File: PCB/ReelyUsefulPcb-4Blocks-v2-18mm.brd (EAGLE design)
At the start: 50 x 86 mm, 28 parts, among them Q1 BSS138, U2 TJCTM240, U3 PHOTON_SMD

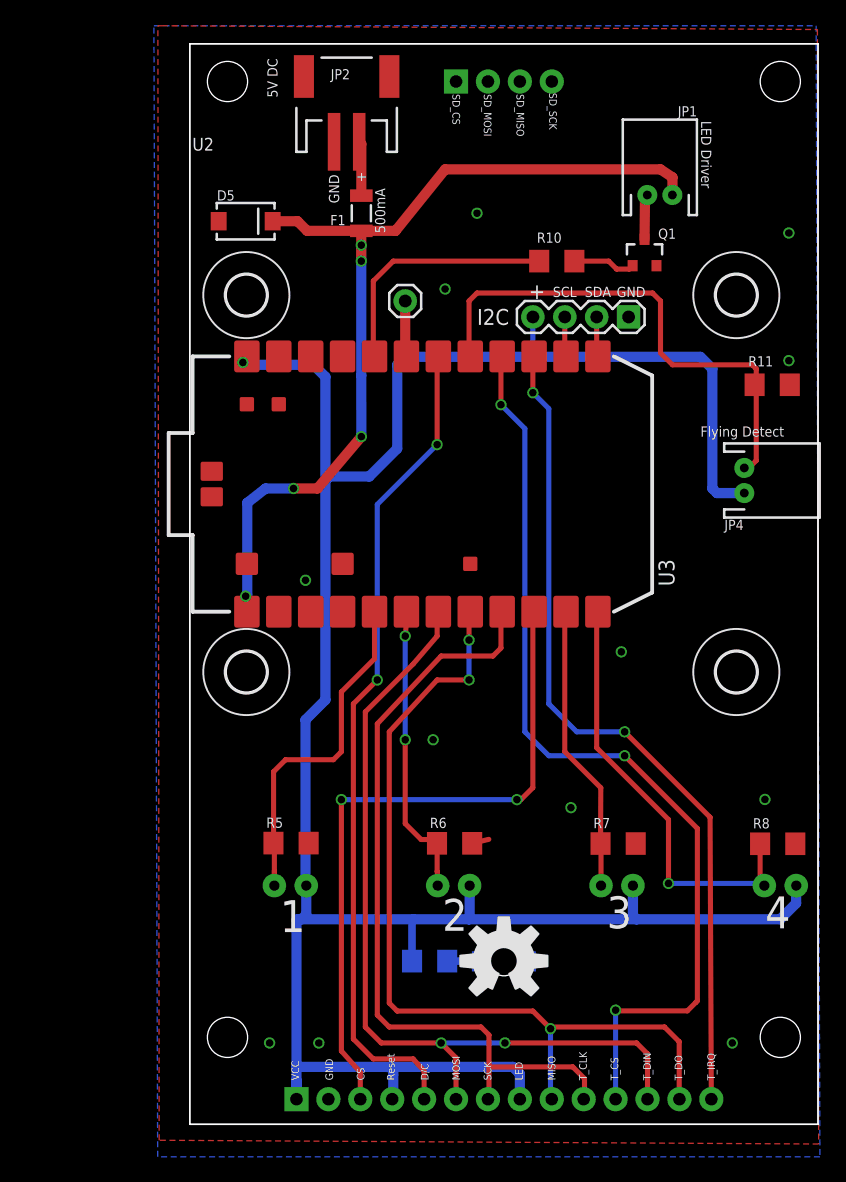
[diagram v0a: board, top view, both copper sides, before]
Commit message: Changed each spool block width to 15mm to give more space for the spools.
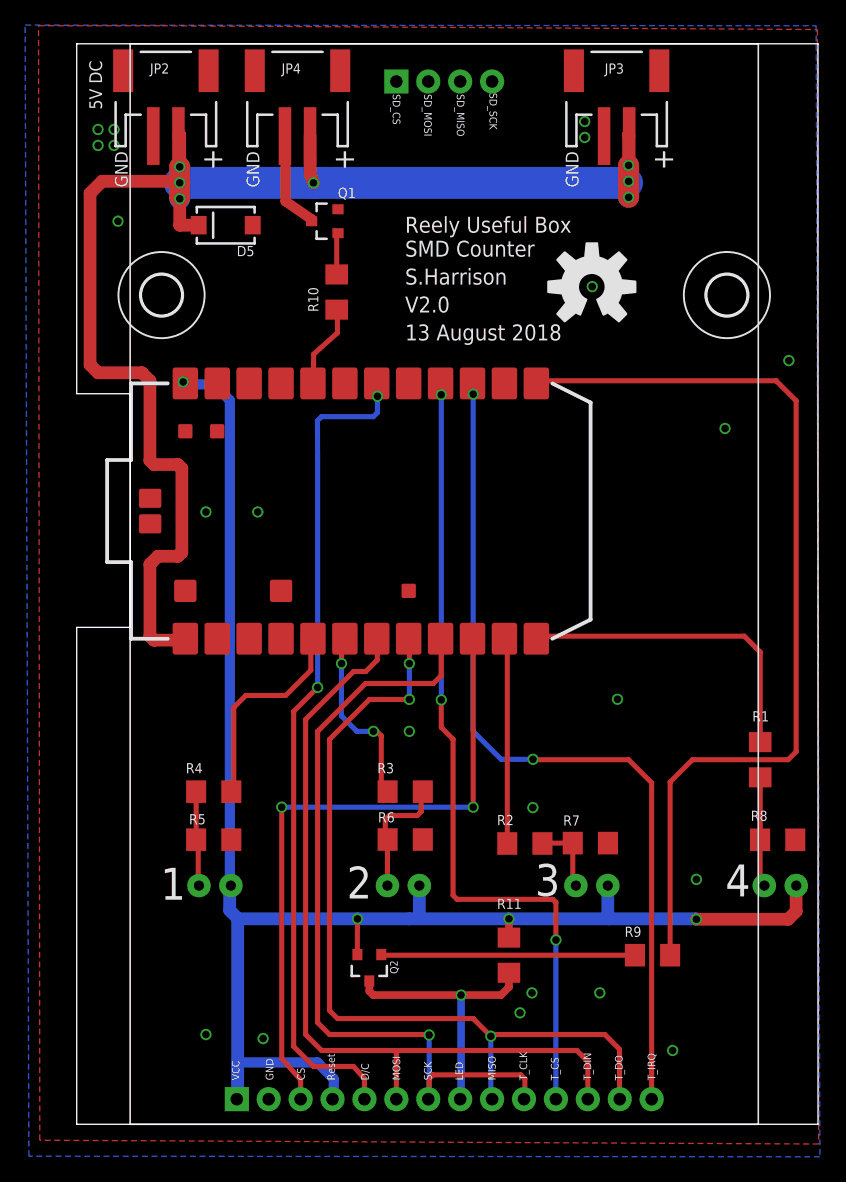
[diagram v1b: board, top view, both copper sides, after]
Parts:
- removed D10: kptd-3216qbc-d-01, SparkFun-LED:LED-1206-BOTTOM
- removed F1: 1206L200PR, SparkFun-PowerIC:PTC-1206
- removed H1, H2: MOUNT-HOLE3.2, holes:3,2
- removed JP1: LED Driver, SparkFun-Connectors:JST-2-PTH
- removed JP6: (no value), SparkFun-Connectors:1X01
- added Q2: 2.5A/30V/105mΩ, SparkFun-DiscreteSemi:SOT23-3
- added R1, R2, R3, R4: 0R, SparkFun-Resistors:1206
- JP3: value i2c -> Power Out; device SparkFun-Connectors:1X04 -> SparkFun-Connectors:JST-2-SMD
- JP4: value Flying detector -> LED Drive; device SparkFun-Connectors:JST-2-PTH -> SparkFun-Connectors:JST-2-SMD
- Q1: device SparkFun-DiscreteSemi:SOT23-3 -> SparkFun-DiscreteSemi:SOT23-3@1
- R11: value 10k -> DNP/0R
- R9: value 1k5 -> 10R
- U2: value TJCTM240 -> TJCTM240NO-MOUNTING-HOMES; device 2.8InchTFT:TJCTM240 -> 2.8InchTFT:TJCTM240-NOHOLES
- moved LOGO1 54.1 mm to (32.0, 50.7)
- moved R11 50.0 mm to (25.4, -2.54), turned to 270 degrees
- moved JP4 47.3 mm to (8.57, 66.4), turned to 0 degrees
- moved Q1 25.5 mm to (10.8, 55.9), turned to 90 degrees
- moved JP3 18.1 mm to (34.0, 66.4), turned to 0 degrees
- moved R9 17.7 mm to (36.8, -2.54), flipped to the top
- moved R10 17.7 mm to (11.7, 50.2), turned to 90 degrees
- moved JP2 14.4 mm to (-1.91, 66.4)
- moved H3 6.75 mm to (-2.25, 50.0)
- moved R5 6.16 mm to (1.91, 6.65)
- moved D1 6.00 mm to (2.00, 3.00)
- moved U3 5.35 mm to (31.9, 22.6)
- moved U2 4.75 mm to (-4.75, -16.0)
- moved D2 4.00 mm to (17.0, 3.00)
- moved R6 3.94 mm to (17.1, 6.67)
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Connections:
- removed net CHANNEL_5_DETECT: JP4.1, R11.2, U3.17
- removed net N$1: D10.A, R9.1
- removed net SCL: JP3.3, U3.14
- removed net SDA: JP3.2, U3.13
- new net CHANNEL_1: D1.A, R4.2, R5.2
- new net CHANNEL_2: D2.A, R3.2, R6.2
- new net CHANNEL_3: D3.A, R2.2, R7.2
- new net CHANNEL_4: D4.A, R1.2, R8.2
- new net DISPLAY_LED_CONTROL: R9.2, U3.13
- net +3V3: now also Q2.2, R11.1; no longer JP3.4, JP4.2, R9.2, U2.LED
- net 5V: now also JP2.2, JP3.2, JP4.2; no longer F1.2, JP1.2
- net CHANNEL_1_DETECT: now also R4.1; no longer D1.A, R5.2
- net CHANNEL_2_DETECT: now also R3.1; no longer D2.A, R6.2
- net CHANNEL_3_DETECT: now also R2.1; no longer D3.A, R7.2
- net CHANNEL_4_DETECT: now also R1.1; no longer D4.A, R8.2
- net GND: no longer D10.C, R11.1
- net N$2: now also JP4.1; no longer JP1.1
- net N$3: now also Q2.1, R9.1; no longer JP6.1, U3.19
- net N$6: now also Q2.3, R11.2, U2.LED; no longer F1.1, JP2.2
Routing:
- net DISPLAY_LED_CONTROL: track 0.00 -> 74.2 mm
- net +3V3: track 197.1 -> 131.6 mm, vias 1 -> 4
- net CHANNEL_5_DETECT: track 41.1 -> 0.00 mm
- net 5V: track 73.9 -> 114.0 mm, vias 5 -> 7
- net N$6: track 4.36 -> 21.7 mm, vias 0 -> 1
- net N$3: track 4.45 -> 20.2 mm
- net LED_CONTROL: track 19.9 -> 6.77 mm
- net CHANNEL_2: track 0.00 -> 10.9 mm
- net CHANNEL_1_DETECT: track 28.6 -> 17.8 mm
- net T_CS: track 75.5 -> 65.5 mm
- net CHANNEL_4_DETECT: track 35.5 -> 25.7 mm, vias 1 -> 0
- net CHANNEL_2_DETECT: track 24.7 -> 15.6 mm
- net CHANNEL_4: track 0.00 -> 8.76 mm
- net CHANNEL_1: track 0.00 -> 7.88 mm
- net CHANNEL_3_DETECT: track 23.0 -> 16.4 mm
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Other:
- board size 50 x 86 mm -> 59 x 86 mm
- board text added: "13 August 2018"
- board text added: "5V DC IN"
- board text added: "5V DC Out"
- board text added: "< Actual dispenser right hand edge (-0.25mm)"
- board text added: "< Right hand edge"
- board text added: "Left hand edge >"
- board text added: "Reely Useful Box"
- board text added: "V2.0"
- board text removed: "14 Jan 2017"
- board text removed: "500mA"
- board text removed: "< Actual dispenser right hand edge"
- board text removed: "Flying Detect"
- board text removed: "I2C"
- board text removed: "SCL"
- board text removed: "SDA"
- board text removed: "V1.0"
